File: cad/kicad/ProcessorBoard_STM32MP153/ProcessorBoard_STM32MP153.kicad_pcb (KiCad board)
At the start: 2 copper layers, 50 x 50 mm, 6 parts, among them J2 SFP, U1 STM32MP153CACx

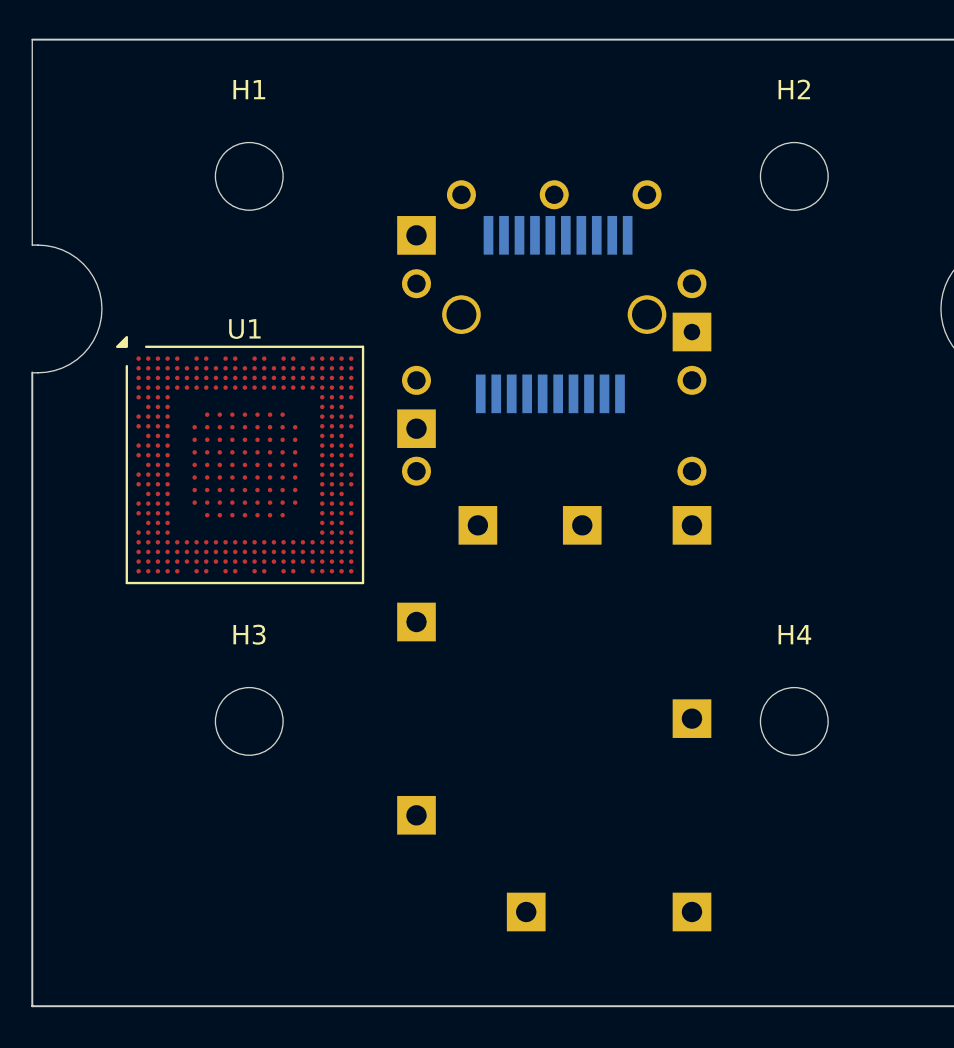
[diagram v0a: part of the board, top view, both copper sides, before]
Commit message: piddling with power
11 distinct power nets out :vine_boom:
5V@8A in :vine_boom:
3v3@3A in :vine_boom:
secure os i2c :vine_boom:

:vine_boom:
:vine_boom:
release me
:vine_boom:

these are absolute maximums the PMIC will need, shouldnt get near them unless the outputs shorted. big step up from the dinky 3v3 mcus :(
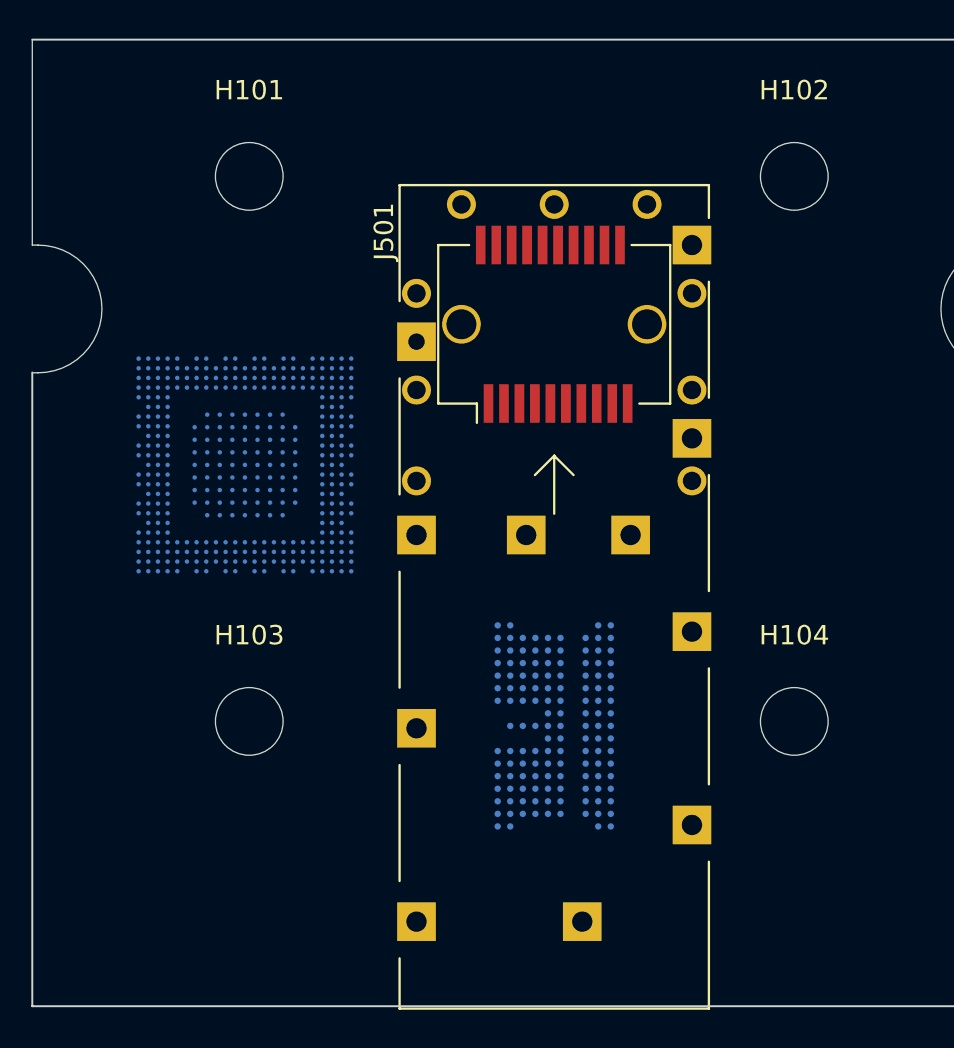
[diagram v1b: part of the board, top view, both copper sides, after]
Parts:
- added IC401: IS43LD16320A-25BLI, __WM_Local:BGA134C65P10X17_1000X1150X110, B.Cu at (157.0, 105.5)
- J501: renamed from J2; moved to F.Cu
- U201: renamed from U1; moved to B.Cu
- moved J501 0.50 mm to (157.0, 78.5)
- turned U201 to 180 degrees
- renumbered H1 to H101, H2 to H102, H3 to H103, H4 to H104
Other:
- copper layers 2 -> 6
- board text added: "maybe we get rid of one of the mounting holes, ddr dosent really fit except on the otherside of the sfp"

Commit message: some more caps and power specs
maybe puppy and rainbows if dont use the sw controlled PMIC. ddr dosent seem to care too much about sequencing, and the mpu sequence is 2 steps... but size :( :( :( . wheres muh leaded puckagies :(
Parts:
- added C301: 10u, Capacitor_SMD:C_0603_1608Metric_Pad1.08x0.95mm_HandSolder, F.Cu at (133.9, 60.7)
- added C302: 22u, Capacitor_SMD:C_0603_1608Metric_Pad1.08x0.95mm_HandSolder, F.Cu at (133.9, 63.2)
- added C303: 10u, Capacitor_SMD:C_0603_1608Metric_Pad1.08x0.95mm_HandSolder, F.Cu at (133.9, 65.7)
- added C304: 22u, Capacitor_SMD:C_0603_1608Metric_Pad1.08x0.95mm_HandSolder, F.Cu at (133.9, 68.2)
- added C305: 10u, Capacitor_SMD:C_0603_1608Metric_Pad1.08x0.95mm_HandSolder, F.Cu at (133.9, 70.7)
- added C306: 22u, Capacitor_SMD:C_0603_1608Metric_Pad1.08x0.95mm_HandSolder, F.Cu at (133.9, 73.2)
- added C307: 10u, Capacitor_SMD:C_0603_1608Metric_Pad1.08x0.95mm_HandSolder, F.Cu at (138.2, 60.7)
- added C308: 22u, Capacitor_SMD:C_0603_1608Metric_Pad1.08x0.95mm_HandSolder, F.Cu at (138.2, 63.2)
- added C309: 10u, Capacitor_SMD:C_0603_1608Metric_Pad1.08x0.95mm_HandSolder, F.Cu at (138.2, 65.7)
- added IC301: STPMIC1BPQR, __WM_Local:QFN40P500X600X80-45N-D, F.Cu at (149.4, 63.5)
- added L301: 1u, Inductor_SMD:L_1008_2520Metric_Pad1.43x2.20mm_HandSolder, F.Cu at (143.1, 61.3)
- added L302: 1u, Inductor_SMD:L_1008_2520Metric_Pad1.43x2.20mm_HandSolder, F.Cu at (143.1, 65.0)
- added L303: 1u, Inductor_SMD:L_1008_2520Metric_Pad1.43x2.20mm_HandSolder, F.Cu at (143.1, 68.8)
- added L304: 1u, Inductor_SMD:L_1008_2520Metric_Pad1.43x2.20mm_HandSolder, F.Cu at (143.1, 72.5)
- added NT301: NetTie_2, NetTie:NetTie-2_SMD_Pad0.5mm, F.Cu at (147.0, 68.5)
- added NT302: NetTie_2, NetTie:NetTie-2_SMD_Pad0.5mm, F.Cu at (147.0, 70.0)
- added NT303: NetTie_2, NetTie:NetTie-2_SMD_Pad0.5mm, F.Cu at (147.0, 71.5)
- added NT304: NetTie_2, NetTie:NetTie-2_SMD_Pad0.5mm, F.Cu at (147.0, 73.0)
- added R301: 3090, Resistor_SMD:R_0603_1608Metric_Pad0.98x0.95mm_HandSolder, F.Cu at (138.2, 68.2)
- added R302: 3090, Resistor_SMD:R_0603_1608Metric_Pad0.98x0.95mm_HandSolder, F.Cu at (138.2, 70.7)
- IC401, U201: moved to F.Cu
- J501: moved to B.Cu
- moved IC401 19.2 mm to (172.0, 93.5), turned to 0 degrees
- turned U201 to 0 degrees
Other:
- copper layers 6 -> 2
- board text removed: "maybe we get rid of one of the mounting holes, ddr dosent really fit except on the otherside of the sfp"

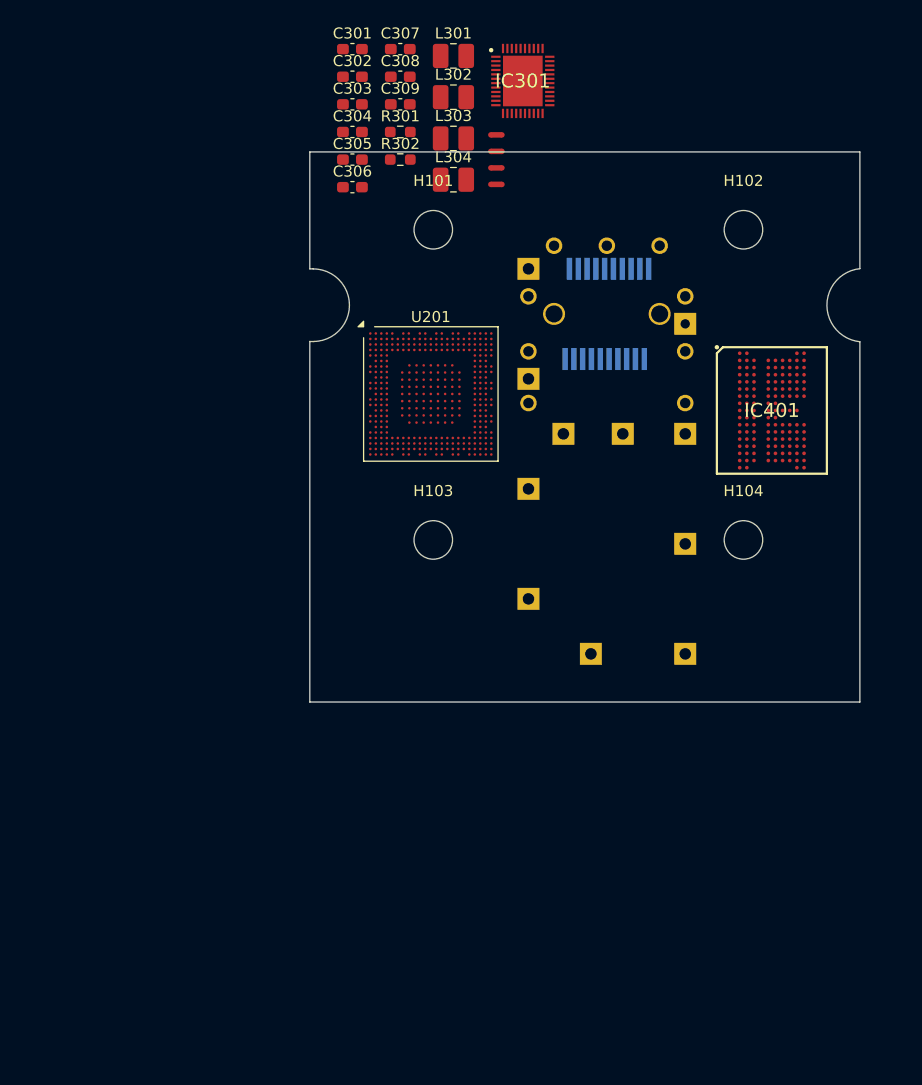
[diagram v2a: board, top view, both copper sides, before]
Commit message: verified jlc price category
~[32, 50]usd for 5 boards. includes impedence control. though must be 1oz top & bottom layers, 0.5oz inner layers . goes up at least $10usd for different pours
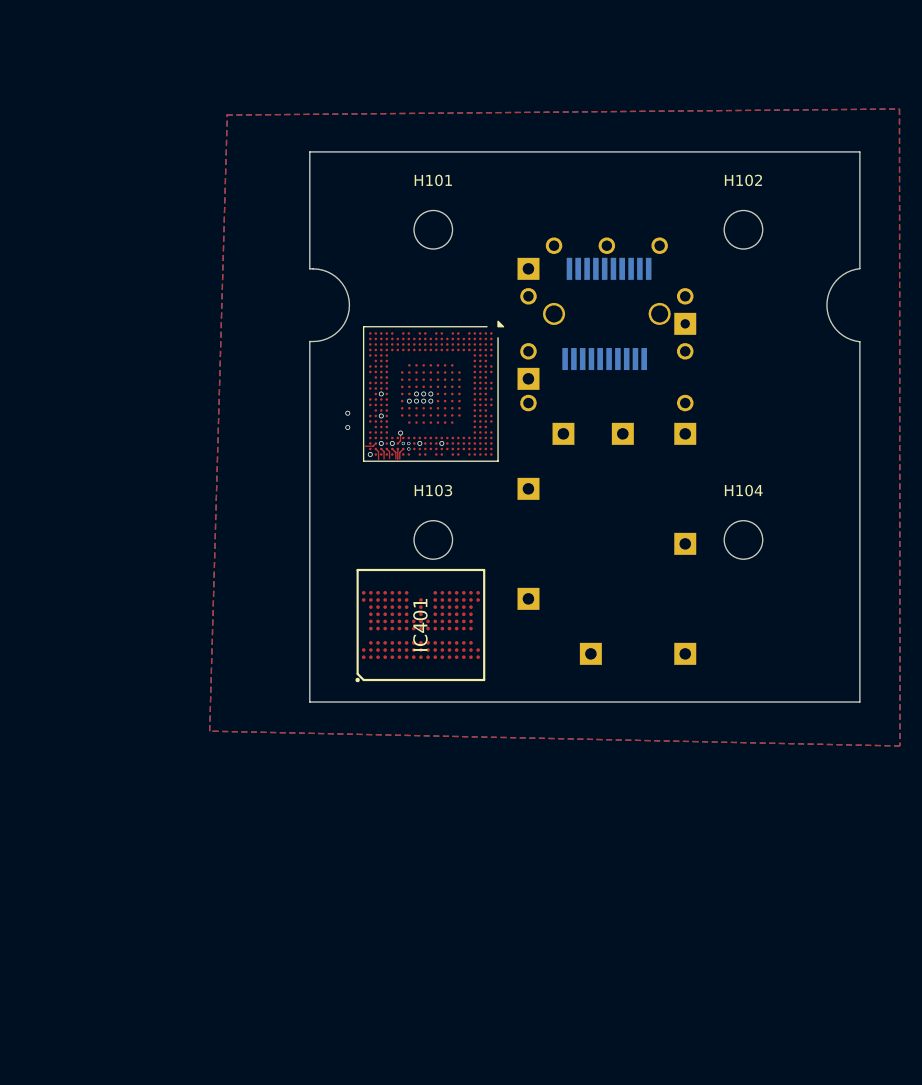
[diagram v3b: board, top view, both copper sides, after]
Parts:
- removed C301, C303, C305, C307, C309: 10u, Capacitor_SMD:C_0603_1608Metric_Pad1.08x0.95mm_HandSolder
- removed C302, C304, C306, C308: 22u, Capacitor_SMD:C_0603_1608Metric_Pad1.08x0.95mm_HandSolder
- removed IC301: STPMIC1BPQR, __WM_Local:QFN40P500X600X80-45N-D
- removed L301, L302, L303, L304: 1u, Inductor_SMD:L_1008_2520Metric_Pad1.43x2.20mm_HandSolder
- removed NT301, NT302, NT303, NT304: NetTie_2, NetTie:NetTie-2_SMD_Pad0.5mm
- removed R301, R302: 3090, Resistor_SMD:R_0603_1608Metric_Pad0.98x0.95mm_HandSolder
- moved IC401 37.4 mm to (140.1, 113.0), turned to 90 degrees
- turned U201 to -90 degrees
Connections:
- U201 pad 1A2: unconnected-(U201-VDDCORE-Pad1A2) -> /V_{dd_core}
- U201 pad 1A3: Net-(U201-VSS-Pad1A3) -> GND
- U201 pad 1A4: unconnected-(U201-VDDCORE-Pad1A4) -> /V_{dd_core}
- U201 pad 1A5: Net-(U201-VSS-Pad1A3) -> GND
- U201 pad 1A6: unconnected-(U201-VDDCORE-Pad1A6) -> /V_{dd_core}
- U201 pad 1A7: Net-(U201-VSS-Pad1A3) -> GND
- U201 pad 1A8: unconnected-(U201-VDDQ_DDR-Pad1A8) -> /V_{dd_DDRQ}
- U201 pad 1B1: unconnected-(U201-VDDCORE-Pad1B1) -> /V_{dd_core}
- U201 pad 1B2: Net-(U201-VSS-Pad1A3) -> GND
- U201 pad 1B3: unconnected-(U201-VDDCORE-Pad1B3) -> /V_{dd_core}
- U201 pad 1B4: Net-(U201-VSS-Pad1A3) -> GND
- U201 pad 1B5: unconnected-(U201-VDDCORE-Pad1B5) -> /V_{dd_core}
- U201 pad 1B6: Net-(U201-VSS-Pad1A3) -> GND
- U201 pad 1B7: unconnected-(U201-VDDQ_DDR-Pad1B7) -> /V_{dd_DDRQ}
- U201 pad 1B8: Net-(U201-VSS-Pad1A3) -> GND
- U201 pad 1B9: unconnected-(U201-VDDQ_DDR-Pad1B9) -> /V_{dd_DDRQ}
- U201 pad 1C1: Net-(U201-VSS-Pad1A3) -> GND
- U201 pad 1C2: unconnected-(U201-VDDCORE-Pad1C2) -> /V_{dd_core}
- U201 pad 1C3: Net-(U201-VSS-Pad1A3) -> GND
- U201 pad 1C4: unconnected-(U201-VDDCORE-Pad1C4) -> /V_{dd_core}
- U201 pad 1C5: Net-(U201-VSS-Pad1A3) -> GND
- U201 pad 1C6: unconnected-(U201-VDDCORE-Pad1C6) -> /V_{dd_core}
- U201 pad 1C7: Net-(U201-VSS-Pad1A3) -> GND
- U201 pad 1C8: unconnected-(U201-VDDQ_DDR-Pad1C8) -> /V_{dd_DDRQ}
- U201 pad 1C9: Net-(U201-VSS-Pad1A3) -> GND
- U201 pad 1D1: unconnected-(U201-VDDCORE-Pad1D1) -> /V_{dd_core}
- U201 pad 1D2: Net-(U201-VSS-Pad1A3) -> GND
- U201 pad 1D3: unconnected-(U201-VDDCORE-Pad1D3) -> /V_{dd_core}
- U201 pad 1D4: Net-(U201-VSS-Pad1A3) -> GND
- U201 pad 1D5: unconnected-(U201-VDDCORE-Pad1D5) -> /V_{dd_core}
- U201 pad 1D6: Net-(U201-VSS-Pad1A3) -> GND
- U201 pad 1D7: unconnected-(U201-VDDCORE-Pad1D7) -> /V_{dd_core}
- U201 pad 1D8: Net-(U201-VSS-Pad1A3) -> GND
- U201 pad 1D9: unconnected-(U201-VDDQ_DDR-Pad1D9) -> /V_{dd_DDRQ}
- U201 pad 1E1: Net-(U201-VSS-Pad1A3) -> GND
- U201 pad 1E2: unconnected-(U201-VDDCORE-Pad1E2) -> /V_{dd_core}
- U201 pad 1E3: Net-(U201-VSS-Pad1A3) -> GND
- U201 pad 1E4: unconnected-(U201-VDDCORE-Pad1E4) -> /V_{dd_core}
- U201 pad 1E5: Net-(U201-VSS-Pad1A3) -> GND
- U201 pad 1E6: unconnected-(U201-VDDCORE-Pad1E6) -> /V_{dd_core}
- U201 pad 1E7: Net-(U201-VSS-Pad1A3) -> GND
- U201 pad 1E8: unconnected-(U201-VDDQ_DDR-Pad1E8) -> /V_{dd_DDRQ}
- U201 pad 1E9: Net-(U201-VSS-Pad1A3) -> GND
- U201 pad 1F2: Net-(U201-VSS-Pad1A3) -> GND
- U201 pad 1F4: Net-(U201-VSS-Pad1A3) -> GND
- U201 pad 1F5: unconnected-(U201-VDDCORE-Pad1F5) -> /V_{dd_core}
- U201 pad 1F6: Net-(U201-VSS-Pad1A3) -> GND
- U201 pad 1F7: unconnected-(U201-VDDCORE-Pad1F7) -> /V_{dd_core}
- U201 pad 1F8: Net-(U201-VSS-Pad1A3) -> GND
- U201 pad 1F9: unconnected-(U201-VDDQ_DDR-Pad1F9) -> /V_{dd_DDRQ}
- U201 pad 1G1: unconnected-(U201-VSS_ANA-Pad1G1) -> GND
- U201 pad 1G3: Net-(U201-VSS-Pad1A3) -> GND
- U201 pad 1G5: Net-(U201-VSS-Pad1A3) -> GND
- U201 pad 1G6: unconnected-(U201-VDDCORE-Pad1G6) -> /V_{dd_core}
- U201 pad 1G7: Net-(U201-VSS-Pad1A3) -> GND
- U201 pad 1G8: unconnected-(U201-VDDQ_DDR-Pad1G8) -> /V_{dd_DDRQ}
- U201 pad 1G9: Net-(U201-VSS-Pad1A3) -> GND
- U201 pad 1H2: unconnected-(U201-VSSA-Pad1H2) -> GND
- U201 pad 1H4: Net-(U201-VSS-Pad1A3) -> GND
- U201 pad 1H6: Net-(U201-VSS-Pad1A3) -> GND
- U201 pad 1H7: unconnected-(U201-VDDCORE-Pad1H7) -> /V_{dd_core}
- U201 pad 1H8: Net-(U201-VSS-Pad1A3) -> GND
- U201 pad 1H9: unconnected-(U201-VDDQ_DDR-Pad1H9) -> /V_{dd_DDRQ}
- U201 pad 1J3: Net-(U201-VSS-Pad1A3) -> GND
- U201 pad 1J5: Net-(U201-VSS-Pad1A3) -> GND
- U201 pad 1J7: Net-(U201-VSS-Pad1A3) -> GND
- U201 pad 1J8: unconnected-(U201-VDDQ_DDR-Pad1J8) -> /V_{dd_DDRQ}
- U201 pad A1: Net-(U201-VSS-Pad1A3) -> GND
- U201 pad A23: Net-(U201-VSS-Pad1A3) -> GND
- U201 pad AA12: Net-(U201-VSS-Pad1A3) -> GND
- U201 pad AA15: unconnected-(U201-VDD3V3_USBHS-PadAA15) -> Net-(U201-VDD3V3_USBFS)
- U201 pad AA16: unconnected-(U201-VSS_USBHS-PadAA16) -> GND
- U201 pad AA17: unconnected-(U201-VDD3V3_USBFS-PadAA17) -> Net-(U201-VDD3V3_USBFS)
- U201 pad AA21: Net-(U201-VSS-Pad1A3) -> GND
- U201 pad AA5: Net-(U201-VSS-Pad1A3) -> GND
- U201 pad AA8: Net-(U201-VSS-Pad1A3) -> GND
- U201 pad AC1: Net-(U201-VSS-Pad1A3) -> GND
- U201 pad AC23: Net-(U201-VSS-Pad1A3) -> GND
- U201 pad C12: Net-(U201-VSS-Pad1A3) -> GND
- U201 pad C16: Net-(U201-VSS-Pad1A3) -> GND
- U201 pad C21: Net-(U201-VSS-Pad1A3) -> GND
- U201 pad C7: Net-(U201-VSS-Pad1A3) -> GND
- U201 pad D4: Net-(U201-VSS-Pad1A3) -> GND
- U201 pad F21: Net-(U201-VSS-Pad1A3) -> GND
- U201 pad H3: Net-(U201-VSS-Pad1A3) -> GND
- U201 pad K21: Net-(U201-VSS-Pad1A3) -> GND
- U201 pad P21: Net-(U201-VSS-Pad1A3) -> GND
- U201 pad P3: Net-(U201-VSS-Pad1A3) -> GND
- U201 pad V21: Net-(U201-VSS-Pad1A3) -> GND
- U201 pad W3: Net-(U201-VSS-Pad1A3) -> GND
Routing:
- net GND: track 0.00 -> 1.05 mm, vias 0 -> 13
- net unconnected-(U201-DDR_DQ26-PadAB21): track 0.00 -> 1.05 mm
- net unconnected-(U201-DDR_DQS3P-PadAB22): track 0.00 -> 1.05 mm
- net unconnected-(U201-DDR_DQS1P-PadU22): track 0.00 -> 1.03 mm
- net unconnected-(U201-DDR_DQ14-PadW22): track 0.00 -> 1.03 mm
- net unconnected-(U201-DDR_DQ31-PadAA22): track 0.00 -> 1.00 mm
- net unconnected-(U201-DDR_DQ25-PadY22): track 0.00 -> 0.95 mm
- net unconnected-(U201-DDR_DQM1-PadV22): track 0.00 -> 0.95 mm
- net unconnected-(U201-DDR_DQ8-PadT21): track 0.00 -> 0.88 mm, vias 0 -> 1
- net unconnected-(U201-DDR_DQ9-PadU21): track 0.00 -> 0.85 mm, vias 0 -> 1
- net unconnected-(U201-DDR_DQ11-PadW21): vias 0 -> 1
- net unconnected-(U201-DDR_DQ10-PadT22): vias 0 -> 1
- net /V_{dd_core}: vias 0 -> 3
- added copper zone on B.Cu, net GND
- added copper zone on F.Cu, net GND
- added copper zone on In1.Cu, net GND
- added copper zone on In2.Cu, net GND
- added copper zone on In3.Cu, net GND
- added copper zone on In4.Cu, net GND
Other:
- copper layers 2 -> 6
